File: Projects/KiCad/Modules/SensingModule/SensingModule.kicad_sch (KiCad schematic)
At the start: 39 parts, among them J1 Conn_01x08, J2 Conn_01x02_Pin, J4 Micro_SD_Card_Det_Hirose_DM3AT, SW1 SW_DIP_x02, U1 MCP2562-E-P, U4 TLP222A, U5 NUCLEO-F303K8, U6 MB85RS2MT, U7 MB85RS2MT

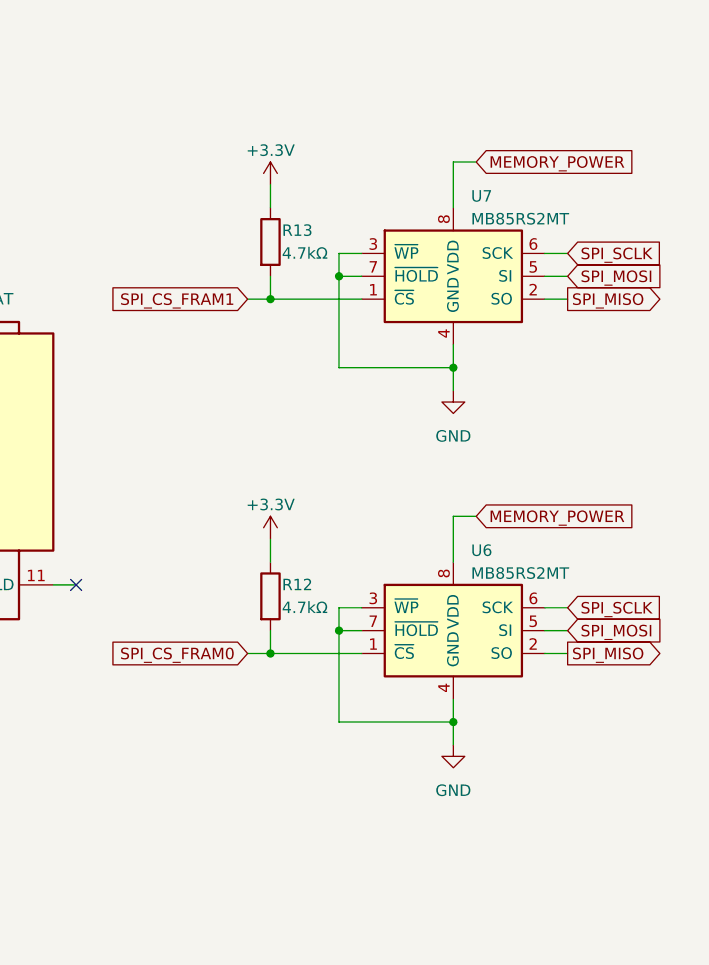
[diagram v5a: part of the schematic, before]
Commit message: FRAMのWPとHOLDをHIGHに固定
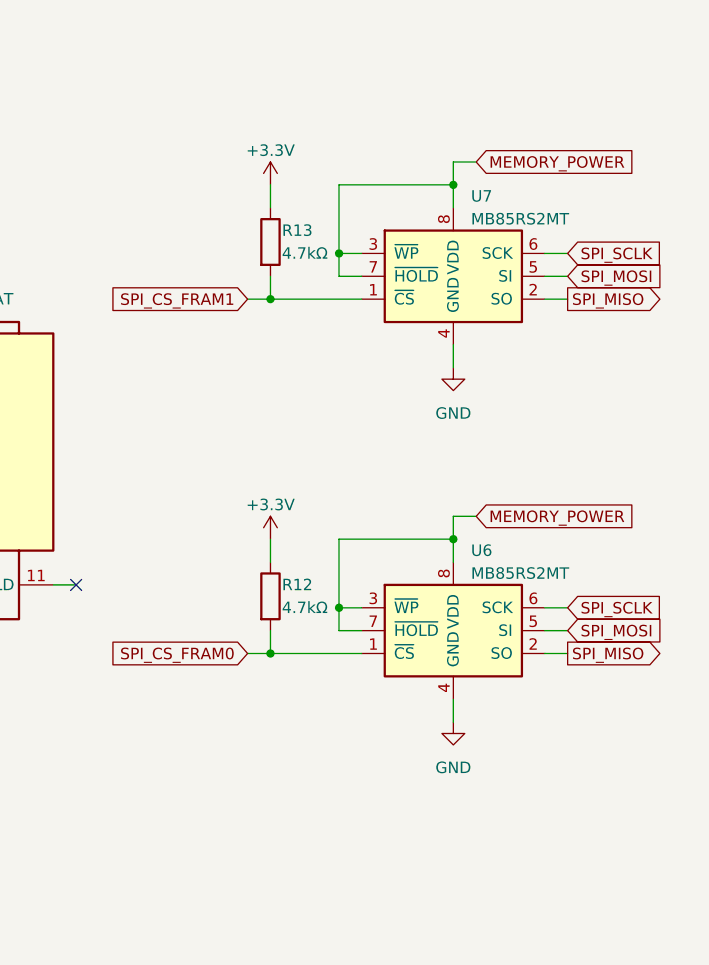
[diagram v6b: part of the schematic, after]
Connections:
- net GND: no longer U6.3 (~{WP}), U6.7 (~{HOLD}), U7.3 (~{WP}), U7.7 (~{HOLD})
- net MEMORY_POWER: now also U6.3 (~{WP}), U6.7 (~{HOLD}), U7.3 (~{WP}), U7.7 (~{HOLD})

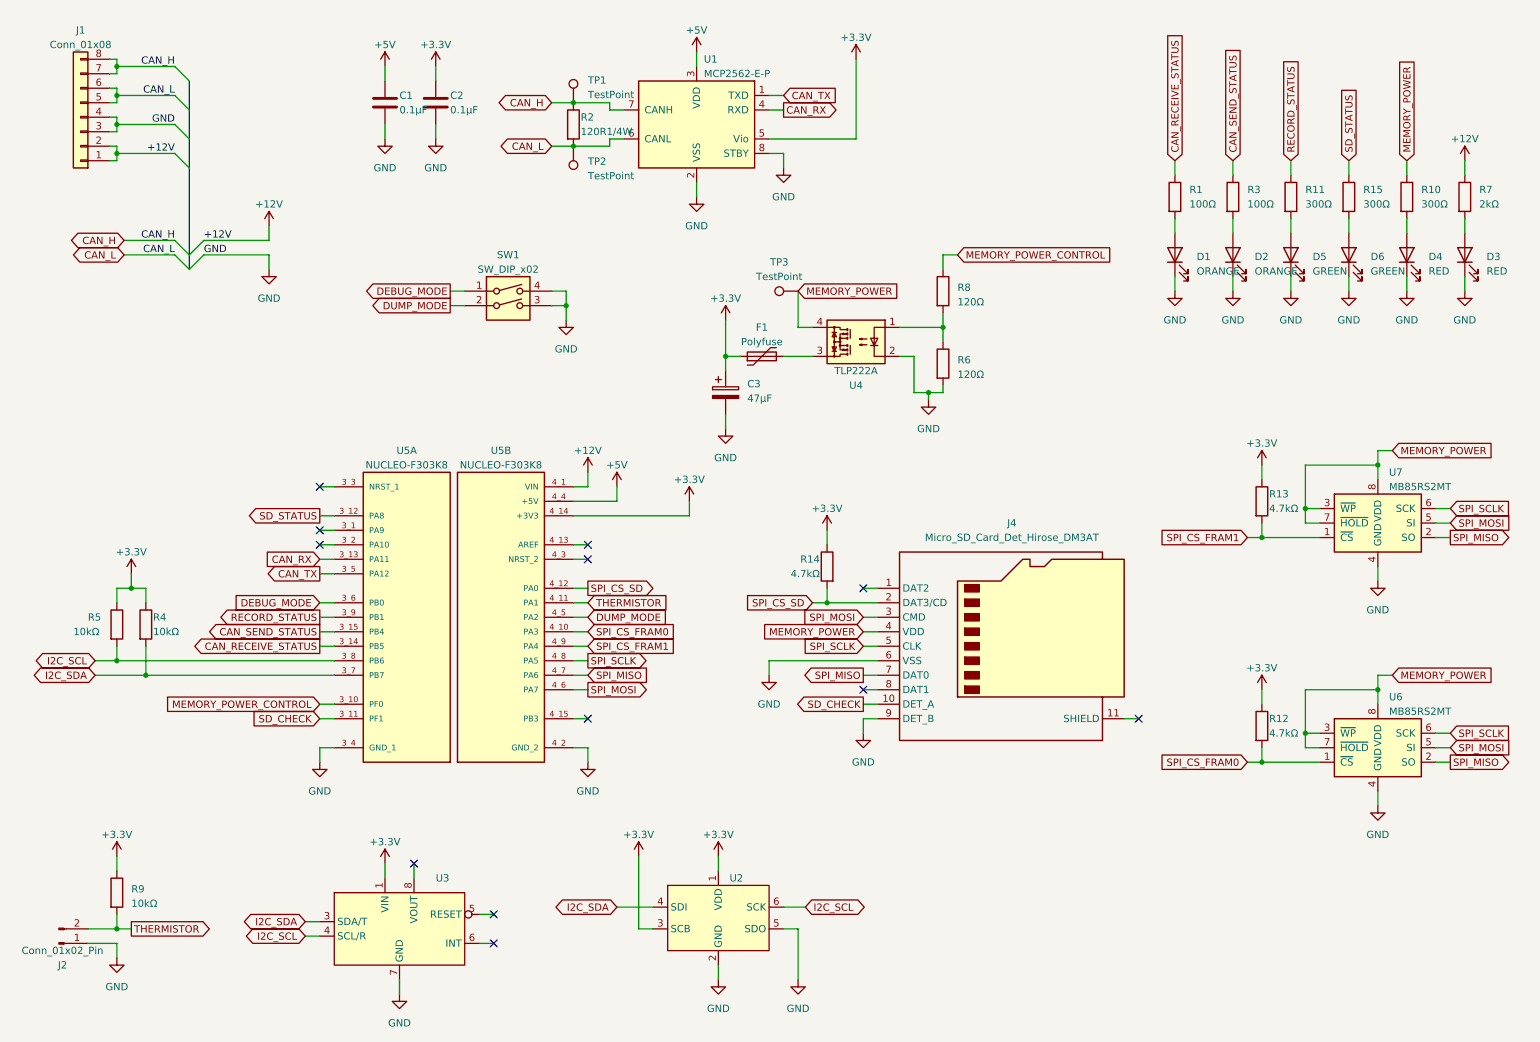
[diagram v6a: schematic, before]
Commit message: 計測モジュールの回路図を分割
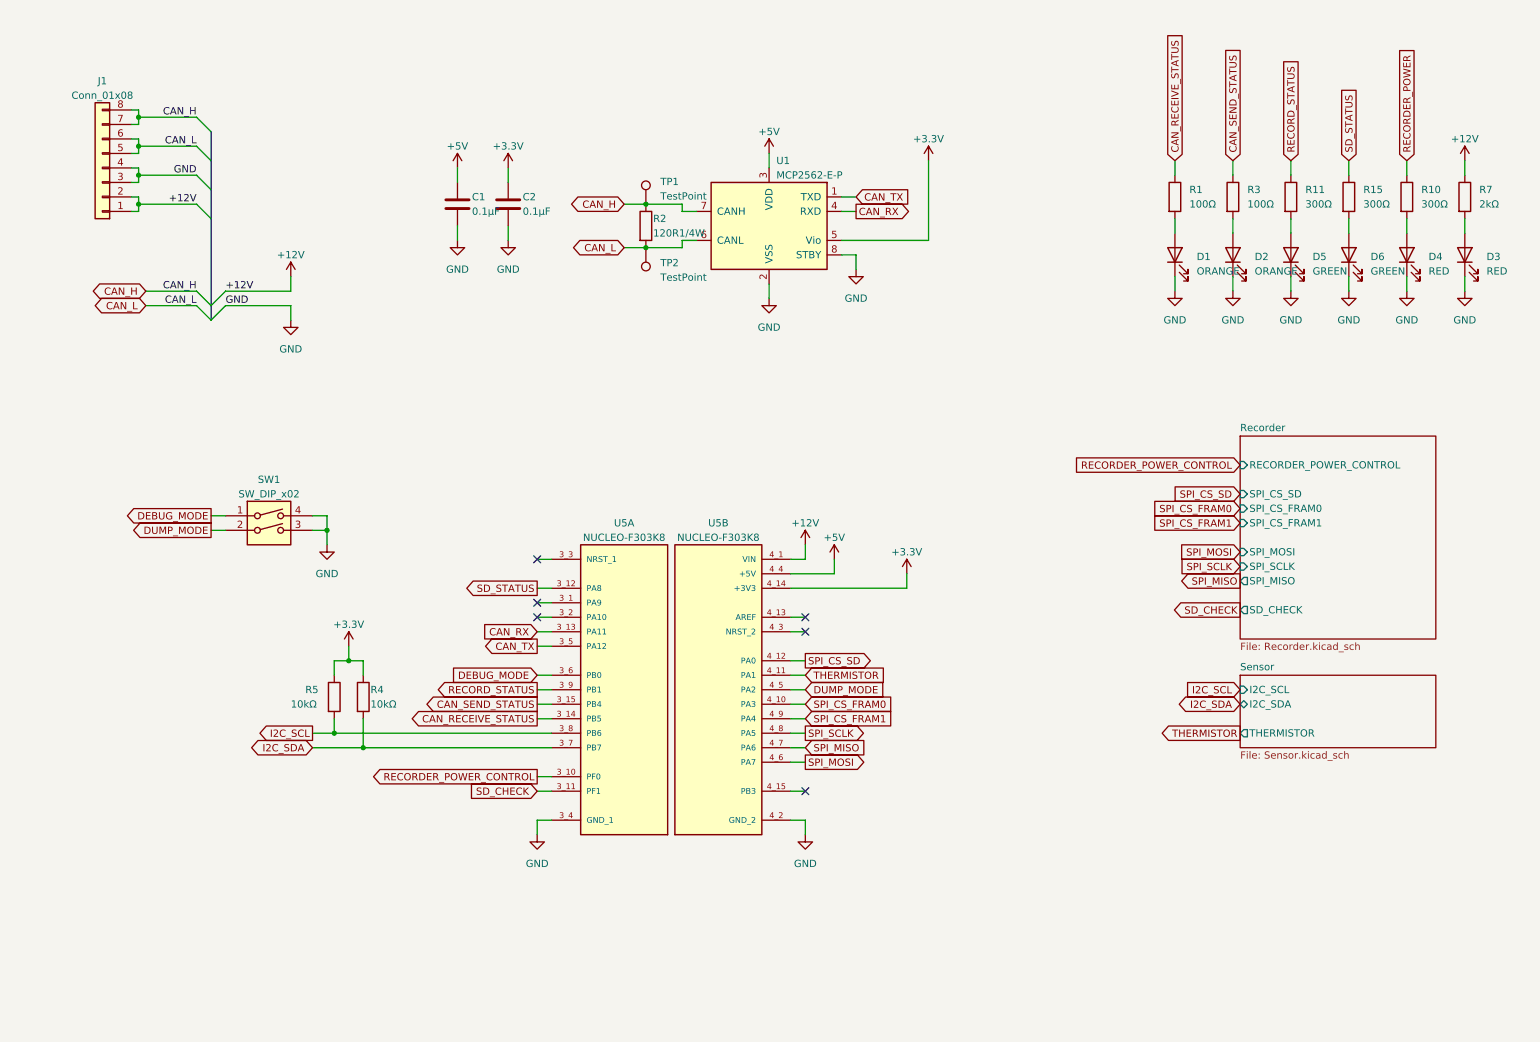
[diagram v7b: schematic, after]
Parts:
- removed C3: 47μF, Capacitor_SMD:CP_Elec_6.3x5.9, symbol Device:C_Polarized
- removed F1: Polyfuse, Fuse:Fuse_1206_3216Metric_Pad1.42x1.75mm_HandSolder, symbol Device:Polyfuse
- removed J2: Conn_01x02_Pin, Hirose_Connector:Hirose_DF1B, symbol Connector:Conn_01x02_Pin
- removed J4: Micro_SD_Card_Det_Hirose_DM3AT, Connector_Card:microSD_HC_Hirose_DM3AT-SF-PEJM5, symbol Connector:Micro_SD_Card_Det_Hirose_DM3AT
- removed R12, R13, R14: 4.7kΩ, Resistor_SMD:R_0603_1608Metric_Pad0.98x0.95mm_HandSolder, symbol Device:R
- removed R6, R8: 120Ω, Resistor_SMD:R_0603_1608Metric_Pad0.98x0.95mm_HandSolder, symbol Device:R
- removed R9: 10kΩ, Resistor_SMD:R_0805_2012Metric_Pad1.20x1.40mm_HandSolder, symbol Device:R
- removed TP3: TestPoint, Connector_Pin:Pin_D1.0mm_L10.0mm, symbol Connector:TestPoint
- removed U2: ~, Akizuki_BME280_Module:BME280, symbol Akizuki_BME280_Module:BME280
- removed U3: ~, Akizuki_BNO055_Module:BNO055, symbol Akizuki_BNO055_Module:BNO055
- removed U4: TLP222A, Package_DIP:DIP-4_W7.62mm, symbol Relay_SolidState:TLP222A
- removed U6, U7: MB85RS2MT, Package_DIP:DIP-8_W7.62mm, symbol Memory_NVRAM:MB85RS2MT
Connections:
- net MEMORY_POWER renamed RECORDER_POWER
- net MEMORY_POWER_CONTROL renamed RECORDER_POWER_CONTROL
- no-connect marks 12 -> 6
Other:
- added sheet Recorder (Recorder.kicad_sch)
- added sheet Sensor (Sensor.kicad_sch)
- moved on the sheet: C1, C2, J1, R2, R4, R5, SW1, TP1, TP2, U1, U5A, U5B

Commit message: ガーバーを再生成
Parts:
- C1, C2: value 0.1μF -> 0.1uF
- D1, D2: value ORANGE -> BLUE
- R1, R3: value 100Ω -> 100R
- R10, R11, R15: value 300Ω -> 300R
- R2: value 120R1/4W -> 120R
- R4, R5: value 10kΩ -> 10kR
- R7: value 2kΩ -> 2kR
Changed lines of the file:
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@@
       (effects (font (size 1.27 1.27)) (justify left))
     )
-    (property "Value" "300Ω" (at 255.27 49.5299 0)
+    (property "Value" "300R" (at 255.27 49.5299 0)
       (effects (font (size 1.27 1.27)) (justify left))
     )
@@
       (effects (font (size 1.27 1.27)) (justify left))
     )
-    (property "Value" "100Ω" (at 234.95 49.5299 0)
+    (property "Value" "100R" (at 234.95 49.5299 0)
       (effects (font (size 1.27 1.27)) (justify left))
     )
@@
       (effects (font (size 1.27 1.27)) (justify left))
     )
-    (property "Value" "2kΩ" (at 275.59 49.5299 0)
+    (property "Value" "2kR" (at 275.59 49.5299 0)
       (effects (font (size 1.27 1.27)) (justify left))
     )
@@
       (effects (font (size 1.27 1.27)) (justify left))
     )
-    (property "Value" "0.1μF" (at 107.95 50.8 0)
+    (property "Value" "0.1uF" (at 107.95 50.8 0)
       (effects (font (size 1.27 1.27)) (justify left))
     )
@@
       (effects (font (size 1.27 1.27)) (justify left))
     )
-    (property "Value" "300Ω" (at 245.11 49.5299 0)
+    (property "Value" "300R" (at 245.11 49.5299 0)
       (effects (font (size 1.27 1.27)) (justify left))
     )
@@
       (effects (font (size 1.27 1.27)) (justify left))
     )
-    (property "Value" "300Ω" (at 265.43 49.5299 0)
+    (property "Value" "300R" (at 265.43 49.5299 0)
       (effects (font (size 1.27 1.27)) (justify left))
     )
@@
       (effects (font (size 1.27 1.27)) (justify left))
     )
-    (property "Value" "0.1μF" (at 99.06 50.8 0)
+    (property "Value" "0.1uF" (at 99.06 50.8 0)
       (effects (font (size 1.27 1.27)) (justify left))
     )
@@
       (effects (font (size 1.27 1.27)) (justify left))
     )
-    (property "Value" "10kΩ" (at 67.31 137.16 0)
+    (property "Value" "10kR" (at 67.31 137.16 0)
       (effects (font (size 1.27 1.27)) (justify left))
     )
@@
       (effects (font (size 1.27 1.27)) (justify right))
     )
-    (property "Value" "ORANGE" (at 226.06 61.2774 90)
+    (property "Value" "BLUE" (at 226.06 61.2774 90)
       (effects (font (size 1.27 1.27)) (justify right))
     )
@@
       (effects (font (size 1.27 1.27)) (justify right))
     )
-    (property "Value" "ORANGE" (at 236.22 61.2774 90)
+    (property "Value" "BLUE" (at 236.22 61.2774 90)
       (effects (font (size 1.27 1.27)) (justify right))
     )
@@
       (effects (font (size 1.27 1.27)) (justify left))
     )
-    (property "Value" "10kΩ" (at 81.28 137.16 0)
+    (property "Value" "10kR" (at 81.28 137.16 0)
       (effects (font (size 1.27 1.27)) (justify left))
     )
@@
       (effects (font (size 1.27 1.27)) (justify left))
     )
-    (property "Value" "100Ω" (at 224.79 49.5299 0)
+    (property "Value" "100R" (at 224.79 49.5299 0)
       (effects (font (size 1.27 1.27)) (justify left))
     )
@@
       (effects (font (size 1.27 1.27)) (justify left))
     )
-    (property "Value" "120R1/4W" (at 130.81 54.61 0)
-      (effects (font (size 1.27 1.27)) (justify left))
-    )
+    (property "Value" "120R" (at 130.81 54.61 0)
+      (effects (font (size 1.27 1.27)) (justify left))
+    )
